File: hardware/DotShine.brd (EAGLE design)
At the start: 30 x 65 mm, 57 parts, among them CN1 1X4-BIG, IC1 CAT24M010TS, IC3 SI1145, J3 USB-MICROB, U1 ATMEGA328P-MU-QFN32, U2 TMP102, U3 ATSHA204-TSU, X2 MC-RTC-RV-4162-C7-I2C, X3 S4B-ZR

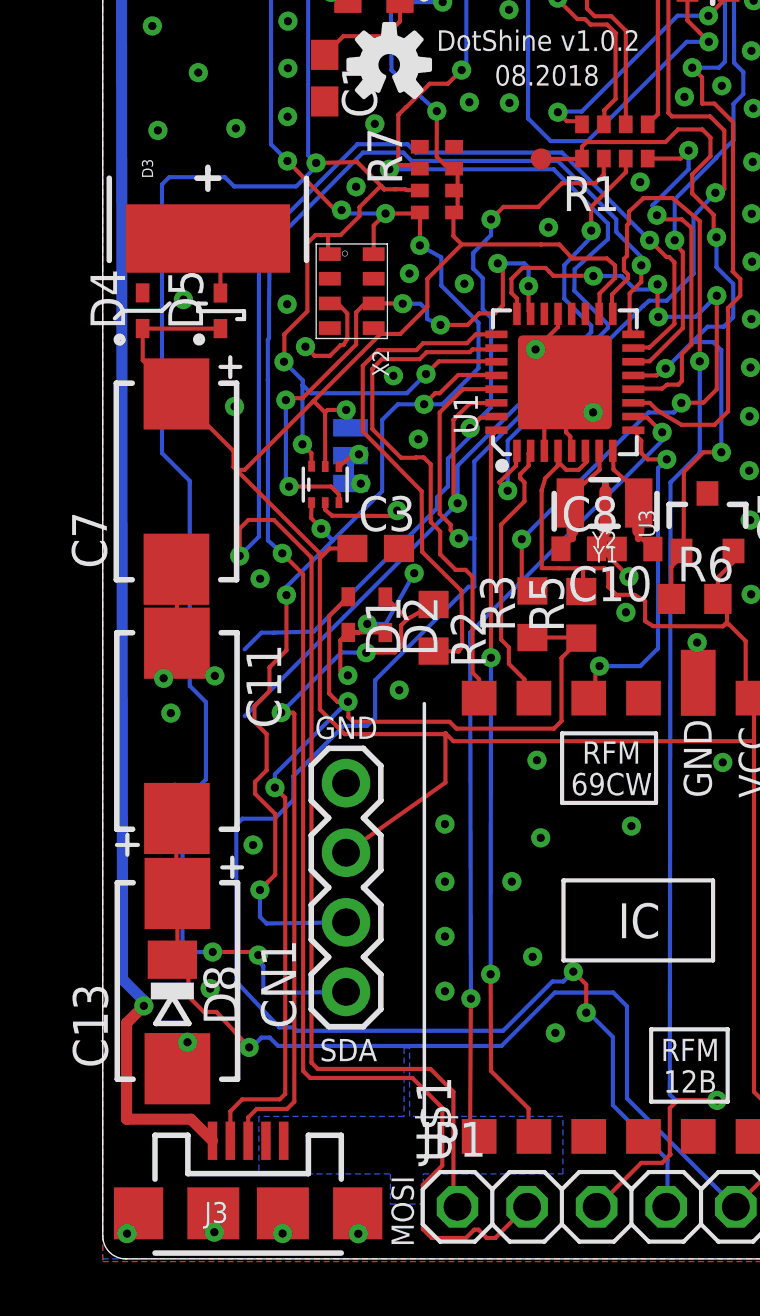
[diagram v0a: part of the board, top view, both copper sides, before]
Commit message: Connect + of solar together, share Schottky
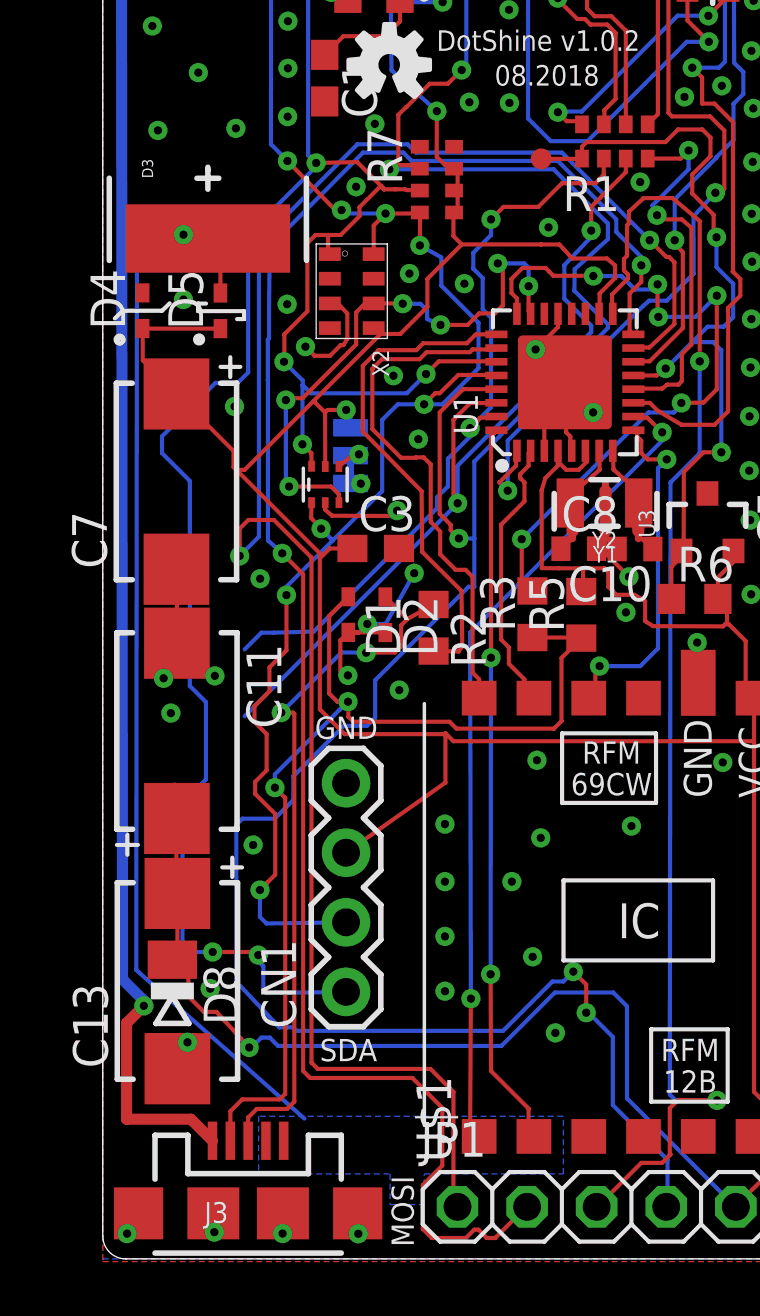
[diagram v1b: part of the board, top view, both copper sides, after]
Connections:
- net N$5 renamed SOLAR_OUT
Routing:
- net SOLAR_OUT: track 2.18 -> 39.6 mm, vias 0 -> 1
- net SDA: track 100.6 -> 97.9 mm
- added copper zone on layer 16, net SOLAR_OUT
- removed copper zone on layer 16, net +3V3
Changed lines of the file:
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@@
 <layer number="19" name="Unrouted" color="6" fill="1" visible="yes" active="yes"/>
 <layer number="20" name="Dimension" color="15" fill="1" visible="yes" active="yes"/>
-<layer number="21" name="tPlace" color="7" fill="1" visible="no" active="yes"/>
-<layer number="22" name="bPlace" color="7" fill="1" visible="no" active="yes"/>
-<layer number="23" name="tOrigins" color="15" fill="1" visible="no" active="yes"/>
-<layer number="24" name="bOrigins" color="15" fill="1" visible="no" active="yes"/>
+<layer number="21" name="tPlace" color="7" fill="1" visible="yes" active="yes"/>
+<layer number="22" name="bPlace" color="7" fill="1" visible="yes" active="yes"/>
+<layer number="23" name="tOrigins" color="15" fill="1" visible="yes" active="yes"/>
+<layer number="24" name="bOrigins" color="15" fill="1" visible="yes" active="yes"/>
 <layer number="25" name="tNames" color="7" fill="1" visible="no" active="yes"/>
 <layer number="26" name="bNames" color="7" fill="1" visible="no" active="yes"/>
@@
 <layer number="40" name="bKeepout" color="1" fill="11" visible="no" active="yes"/>
 <layer number="41" name="tRestrict" color="4" fill="10" visible="no" active="yes"/>
-<layer number="42" name="bRestrict" color="1" fill="10" visible="no" active="yes"/>
-<layer number="43" name="vRestrict" color="2" fill="10" visible="no" active="yes"/>
+<layer number="42" name="bRestrict" color="1" fill="10" visible="yes" active="yes"/>
+<layer number="43" name="vRestrict" color="2" fill="10" visible="yes" active="yes"/>
 <layer number="44" name="Drills" color="7" fill="1" visible="no" active="yes"/>
 <layer number="45" name="Holes" color="7" fill="1" visible="no" active="yes"/>
@@
 <wire x1="3.177" y1="20.915" x2="3.177" y2="28.4" width="0.1524" layer="16"/>
 <wire x1="3.177" y1="28.4" x2="2.162" y2="29.415" width="0.1524" layer="16"/>
-<wire x1="2.162" y1="29.415" x2="2.162" y2="39.224" width="0.1524" layer="16"/>
-<wire x1="2.162" y1="39.224" x2="2.427" y2="39.489" width="0.1524" layer="16"/>
-<wire x1="2.427" y1="39.489" x2="4.457" y2="39.489" width="0.1524" layer="16"/>
-<wire x1="4.457" y1="39.489" x2="4.795" y2="39.151" width="0.1524" layer="16"/>
-<wire x1="4.795" y1="39.151" x2="7.06" y2="39.151" width="0.1524" layer="16"/>
-<wire x1="7.06" y1="39.151" x2="7.78966875" y2="39.88066875" width="0.1524" layer="16"/>
 <wire x1="7.78966875" y1="39.88066875" x2="7.78966875" y2="40.0072875" width="0.1524" layer="16"/>
 <wire x1="14.301" y1="51.642" x2="11.373" y2="51.642" width="0.1524" layer="1"/>
@@
 <wire x1="4.0132" y1="11.2014" x2="3.0656" y2="11.2014" width="0.1524" layer="16"/>
 <wire x1="3.0656" y1="11.2014" x2="2.912" y2="11.355" width="0.1524" layer="16"/>
+<wire x1="2.162" y1="29.415" x2="2.162" y2="30.0258" width="0.1524" layer="16"/>
+<wire x1="2.162" y1="30.0258" x2="4.1148" y2="31.9786" width="0.1524" layer="16"/>
+<wire x1="4.1148" y1="31.9786" x2="4.9276" y2="31.9786" width="0.1524" layer="16"/>
+<wire x1="4.9276" y1="31.9786" x2="5.3086" y2="32.3596" width="0.1524" layer="16"/>
+<wire x1="5.3086" y1="32.3596" x2="5.3086" y2="37.3996" width="0.1524" layer="16"/>
+<wire x1="5.3086" y1="37.3996" x2="7.78966875" y2="39.88066875" width="0.1524" layer="16"/>
 </signal>
 <signal name="RST">
@@
 <wire x1="16.504" y1="9.722" x2="14.5544" y2="7.7724" width="0.1524" layer="16"/>
 <wire x1="14.5544" y1="7.7724" x2="6.4008" y2="7.7724" width="0.1524" layer="16"/>
-<polygon width="0.1524" layer="16" isolate="0.1" orphans="yes">
-<vertex x="5.7" y="3.1"/>
-<vertex x="10.5" y="3.1"/>
-<vertex x="10.5" y="2"/>
-<vertex x="11.7" y="2"/>
-<vertex x="11.7" y="3.1"/>
-<vertex x="16.8" y="3.1"/>
-<vertex x="16.8" y="5.2"/>
-<vertex x="11.2" y="5.2"/>
-<vertex x="11.2" y="7.7"/>
-<vertex x="11" y="7.7"/>
-<vertex x="11" y="5.2"/>
-<vertex x="5.7" y="5.2"/>
-</polygon>
 <wire x1="5.652840625" y1="61.727840625" x2="4.925" y2="61" width="0.1524" layer="16"/>
 <wire x1="4.925" y1="61" x2="3.5" y2="61" width="0.1524" layer="16"/>
@@
 <wire x1="22.845" y1="46.115" x2="22.11" y2="45.38" width="0.1524" layer="1"/>
 </signal>
-<signal name="N$5">
+<signal name="SOLAR_OUT">
 <contactref element="D3" pad="+"/>
 <contactref element="D5" pad="A"/>
 <wire x1="4.296" y1="35.26" x2="4.296" y2="36.791" width="0.1524" layer="1"/>
 <wire x1="4.296" y1="36.791" x2="3.837" y2="37.25" width="0.1524" layer="1"/>
+<polygon width="0.1524" layer="16" orphans="yes">
+<vertex x="5.6896" y="5.207"/>
+<vertex x="5.6896" y="3.0988"/>
+<vertex x="10.4902" y="3.0988"/>
+<vertex x="10.4902" y="1.9812"/>
+<vertex x="11.7348" y="1.9812"/>
+<vertex x="11.7348" y="3.0988"/>
+<vertex x="16.8148" y="3.0988"/>
+<vertex x="16.8148" y="5.207"/>
+</polygon>
+<wire x1="1.2226" y1="10.5458" x2="1.248" y2="36.9942" width="0.1524" layer="16"/>
+<wire x1="1.248" y1="36.9942" x2="1.6426" y2="37.3888" width="0.1524" layer="16"/>
+<wire x1="1.6426" y1="37.3888" x2="2.9464" y2="37.3888" width="0.1524" layer="16"/>
+<via x="2.9464" y="37.3888" extent="1-16" drill="0.3"/>
+<wire x1="2.9464" y1="37.3888" x2="3.0852" y2="37.25" width="0.1524" layer="1"/>
+<wire x1="3.0852" y1="37.25" x2="3.837" y2="37.25" width="0.1524" layer="1"/>
+<wire x1="1.3428" y1="10.4346" x2="7.3626" y2="5.119" width="0.1524" layer="16"/>
+<wire x1="1.3428" y1="10.4346" x2="1.2316" y2="10.5458" width="0.1524" layer="16"/>
+<wire x1="1.2316" y1="10.5458" x2="1.2226" y2="10.5458" width="0.1524" layer="16"/>
 </signal>
 <signal name="INT_MULTIPLE">
@@
 <wire x1="10.85" y1="45.178" x2="10.85" y2="46.185" width="0.1524" layer="1"/>
 </signal>
+<signal name="N$5">
+</signal>
+<signal name="N$33">
+</signal>
 </signals>

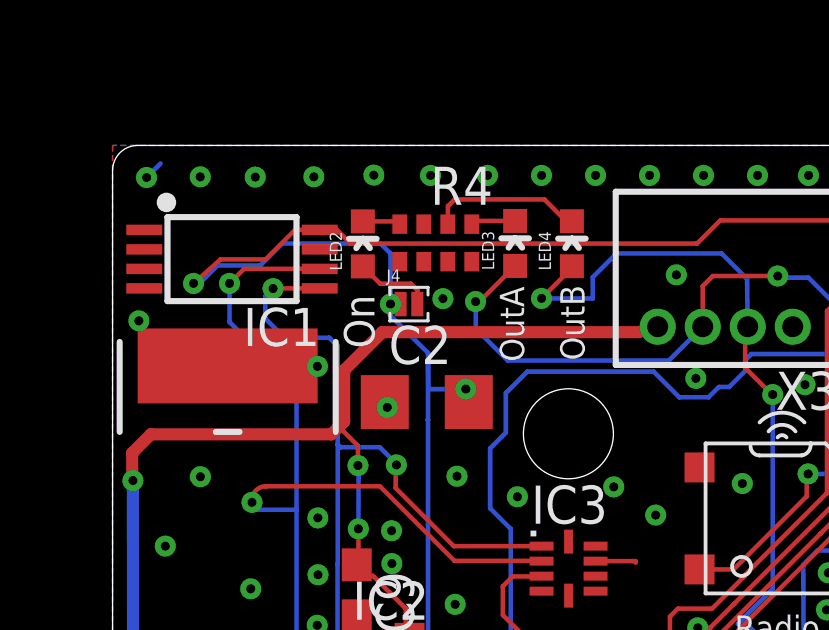
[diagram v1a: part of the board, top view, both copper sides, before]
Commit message: On Led -> USB, now at 5V. Only on when usb present
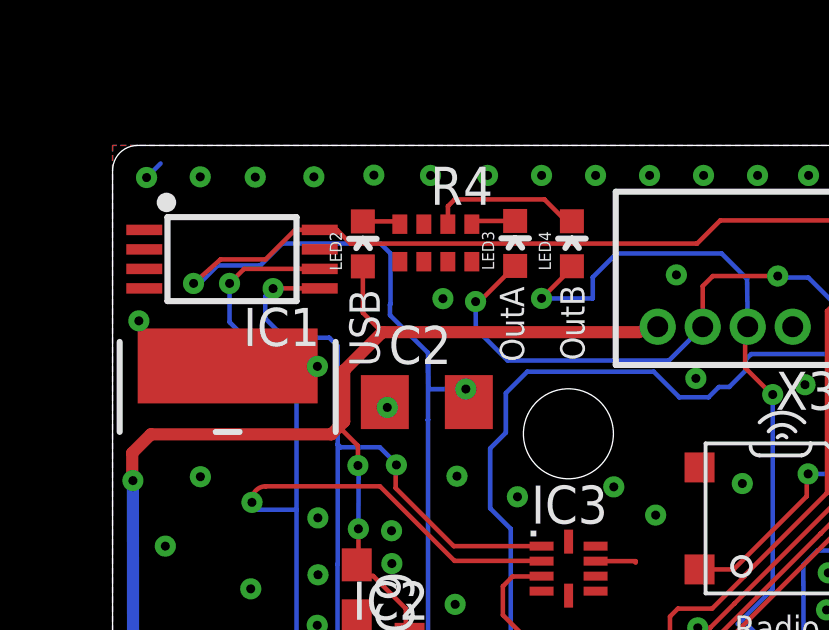
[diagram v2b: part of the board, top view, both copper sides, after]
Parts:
- removed J4: (no value), solderjumper:2.MED
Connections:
- removed net N$12: J4.2, LED2.A
- net +3V3: no longer J4.1
- net +5V: now also LED2.A
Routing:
- net +5V: track 84.1 -> 87.1 mm
- net N$12: track 2.61 -> 0.00 mm
- net +3V3: track 237.3 -> 237.0 mm, vias 9 -> 8
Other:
- board text added: "USB"
- board text removed: "On"
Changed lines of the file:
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@@
 <text x="13.721525" y="57.79208125" size="0.8128" layer="21" rot="R90">OutA</text>
 <text x="15.735996875" y="57.836234375" size="0.8128" layer="21" rot="R90">OutB</text>
-<text x="8.730875" y="58.235671875" size="1.016" layer="21" rot="R90">On</text>
+<text x="8.908675" y="57.626071875" size="1.016" layer="21" rot="R90">USB</text>
 <text x="10.01839375" y="8.028075" size="0.8128" layer="21" rot="R180">SDA</text>
 <text x="10.042053125" y="19.794415625" size="0.8128" layer="21" rot="R180">GND</text>
@@
 <element name="IC2" library="MCP1700" package="SOT-23" value="" x="9.9" y="47.285"/>
 <element name="C9" library="rcl" package="C0603" value="1uF" x="8.14" y="50.17" rot="R270"/>
-<element name="J4" library="solderjumper" package="2.MED" value="" x="9.88" y="59.71"/>
 <element name="LED5" library="SparkFun" package="LED-0603" value="" x="22.065" y="47.71" rot="R270"/>
 <element name="LED6" library="SparkFun" package="LED-0603" value="" x="22.095" y="46.29" rot="R270"/>
@@
 <wire x1="9.247621875" y1="59.3412" x2="9.245396875" y2="59.691015625" width="0.1524" layer="16"/>
 <wire x1="9.245396875" y1="59.691015625" x2="9.26490625" y2="59.71336875" width="0.1524" layer="16"/>
-<via x="9.26490625" y="59.71336875" extent="1-16" drill="0.3"/>
 <contactref element="U3" pad="2"/>
 <wire x1="23.025390625" y1="25.84195625" x2="23.131775" y2="25.55138125" width="0.1524" layer="1"/>
@@
 <wire x1="11.85" y1="34.755" x2="11.85" y2="35.7768" width="0.1524" layer="1"/>
 <wire x1="11.85" y1="35.7768" x2="13.1064" y2="37.0332" width="0.1524" layer="1"/>
-<contactref element="J4" pad="1"/>
-<wire x1="9.6006" y1="59.71336875" x2="9.6006" y2="59.71" width="0.1524" layer="1"/>
 <wire x1="9.26490625" y1="59.71336875" x2="9.26490625" y2="61.397934375" width="0.1524" layer="16"/>
 <wire x1="9.26490625" y1="61.397934375" x2="8.935" y2="61.727840625" width="0.1524" layer="16"/>
@@
 <wire x1="2.216" y1="11.203" x2="2.725" y2="11.203" width="0.1524" layer="1"/>
 <wire x1="2.725" y1="11.203" x2="2.725" y2="13.34" width="0.1524" layer="1"/>
-<wire x1="9.6006" y1="59.71" x2="9.26490625" y2="59.71" width="0.1524" layer="1"/>
-<wire x1="9.26490625" y1="59.71" x2="9.26490625" y2="59.71336875" width="0.1524" layer="1"/>
 </signal>
 <signal name="ADCENA">
@@
 <wire x1="1.5" y1="9.236" x2="1.5" y2="9.426" width="0.4064" layer="16"/>
 <wire x1="1.5" y1="9.426" x2="0.721" y2="10.205" width="0.4064" layer="16"/>
+<wire x1="8.9906" y1="58.7746" x2="9.6006" y2="58.7746" width="0.1524" layer="1"/>
+<contactref element="LED2" pad="A"/>
+<wire x1="8.343165625" y1="60.967659375" x2="8.343165625" y2="59.422034375" width="0.1524" layer="1"/>
+<wire x1="8.343165625" y1="59.422034375" x2="8.9906" y2="58.7746" width="0.1524" layer="1"/>
 </signal>
 <signal name="N$7">
@@
 <wire x1="9.25" y1="34.564" x2="9.271" y2="34.574" width="0" layer="19" extent="1-1"/>
 </signal>
-<signal name="N$12">
-<contactref element="LED2" pad="A"/>
-<contactref element="J4" pad="2"/>
-<wire x1="10.1594" y1="59.71" x2="10.1594" y2="60.1756" width="0.1524" layer="1"/>
-<wire x1="10.1594" y1="60.1756" x2="9.945" y2="60.39" width="0.1524" layer="1"/>
-<wire x1="9.945" y1="60.39" x2="8.920825" y2="60.39" width="0.1524" layer="1"/>
-<wire x1="8.920825" y1="60.39" x2="8.343165625" y2="60.967659375" width="0.1524" layer="1"/>
-</signal>
 <signal name="N$13">
